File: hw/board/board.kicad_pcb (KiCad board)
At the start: 4 copper layers, 100 x 85 mm, 77 parts, among them J1 Conn_ARM_JTAG_SWD_10, J2 Conn_ARM_JTAG_SWD_10, SW1 TSB008A2526A, SW2 TSB008A2526A, U1 STM32F302CBTx, U2 W25Q128JVSIQTR, U3 AP7361C-18SP-13, U4 AP7361C-10E, U5 TPS54331DR, U6 XC7A35T-FTG256

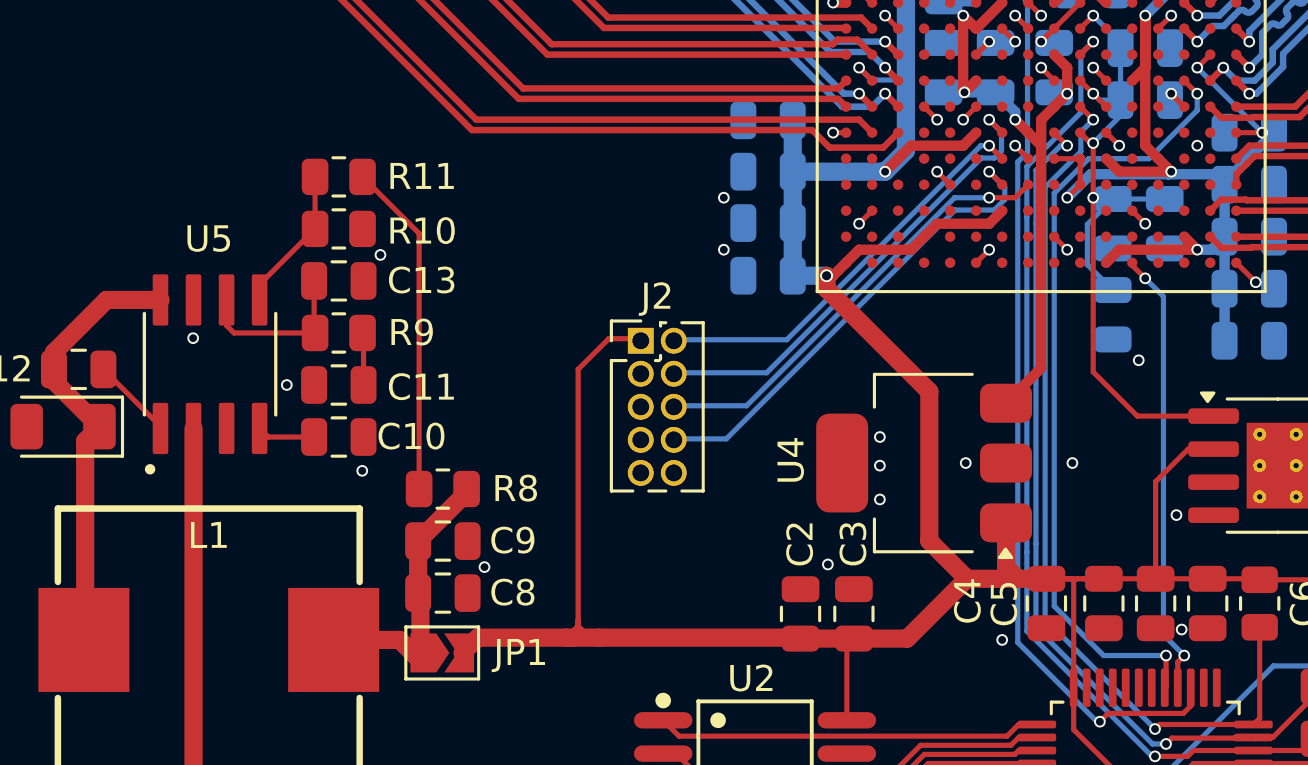
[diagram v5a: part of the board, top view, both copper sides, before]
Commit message: Fixed silkscreen overlaps, updated verilator shims
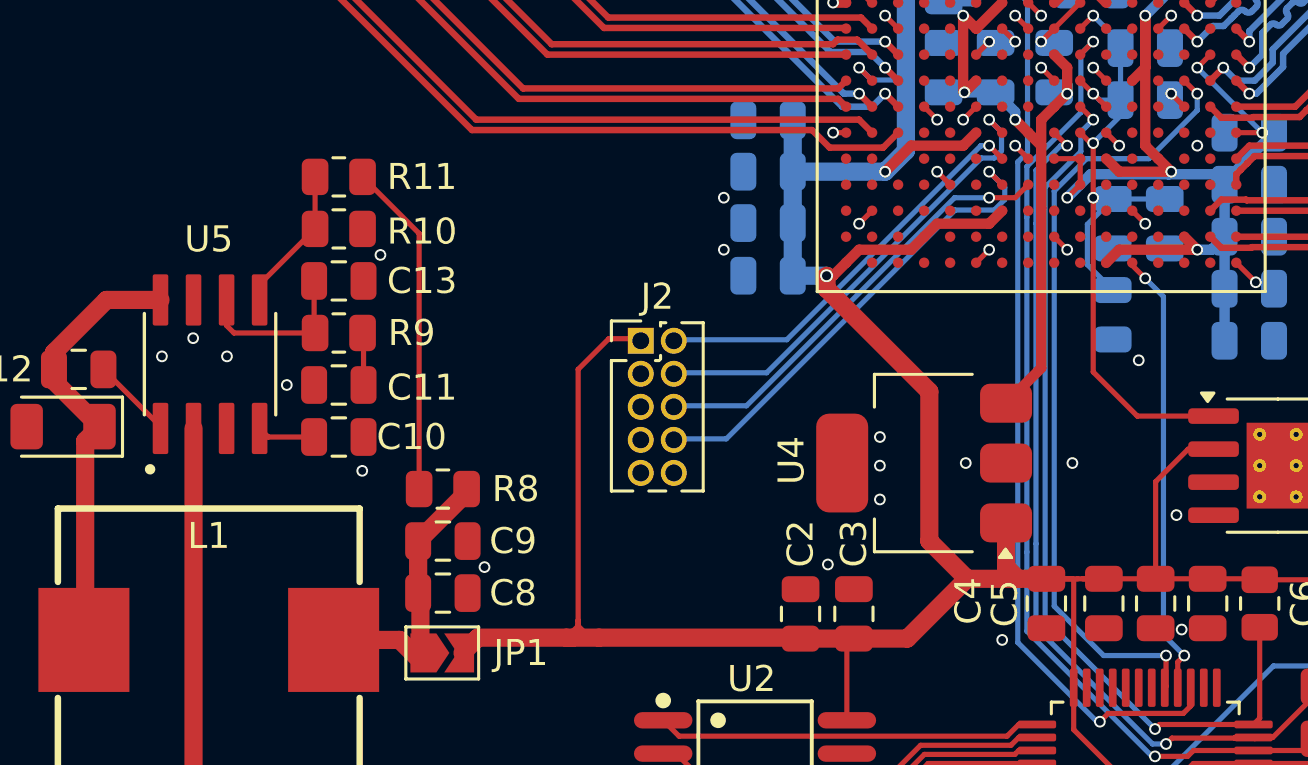
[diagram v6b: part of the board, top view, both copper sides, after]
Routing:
- net GND: vias 55 -> 57
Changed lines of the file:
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@@
 		(tags "capacitor")
 		(property "Reference" "C19"
-			(at 2.75 0 90)
+			(at 3.5 0 90)
 			(layer "B.SilkS")
 			(effects
@@
 		(tags "capacitor")
 		(property "Reference" "C17"
-			(at 2.75 0 0)
+			(at 3.2 0 0)
 			(layer "B.SilkS")
 			(effects
@@
 	)
 	(via
+		(at 102.7 84.1)
+		(size 0.45)
+		(drill 0.3)
+		(layers "F.Cu" "B.Cu")
+		(free yes)
+		(net 5)
+	)
+	(via
 		(at 134 71)
 		(size 0.45)
@@
 	)
 	(via
+		(at 100.2 84.1)
+		(size 0.45)
+		(drill 0.3)
+		(layers "F.Cu" "B.Cu")
+		(free yes)
+		(net 5)
+	)
+	(via
 		(at 147 103.8)
 		(size 0.45)
@@
 	)
 	(segment
-		(start 138.139033 76.5)
-		(end 140 74.639033)
+		(start 135.744974 76.5)
+		(end 138.139033 76.5)
 		(width 0.2)
 		(layer "B.Cu")
@@
 	)
 	(segment
-		(start 138.8 95.6)
-		(end 136.4 95.6)
+		(start 134.5 77.744974)
+		(end 135.744974 76.5)
 		(width 0.2)
 		(layer "B.Cu")
@@
 	)
 	(segment
-		(start 140 74.639033)
-		(end 140 74)
+		(start 138.139033 76.5)
+		(end 140 74.639033)
 		(width 0.2)
 		(layer "B.Cu")
@@
 	)
 	(segment
-		(start 134.5 93.7)
-		(end 134.5 77.828248)
+		(start 138.8 95.6)
+		(end 136.4 95.6)
 		(width 0.2)
 		(layer "B.Cu")
@@
 	)
 	(segment
-		(start 135.828248 76.5)
-		(end 138.139033 76.5)
+		(start 140 74.639033)
+		(end 140 74)
 		(width 0.2)
 		(layer "B.Cu")
@@
 	)
 	(segment
-		(start 134.5 77.828248)
-		(end 135.828248 76.5)
+		(start 134.5 93.7)
+		(end 134.5 77.744974)
 		(width 0.2)
 		(layer "B.Cu")

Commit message: Updated net names for SPI bitstream upload
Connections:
- net CCLK renamed FPGA_CCLK
- net DIN renamed FPGA_DIN
- net DOUT renamed FPGA_DOUT
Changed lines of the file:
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@@
 	(net 40 "unconnected-(U1-PF1-Pad6)")
 	(net 41 "S_{out}5_N")
-	(net 42 "DOUT")
+	(net 42 "FPGA_DOUT")
 	(net 43 "D_{out}5_P")
-	(net 44 "DIN")
+	(net 44 "FPGA_CCLK")
 	(net 45 "unconnected-(U1-PC15-Pad4)")
 	(net 46 "unconnected-(U1-PB7-Pad43)")
@@
 	(net 76 "S_{in}6_P")
 	(net 77 "unconnected-(U6A-IO_L1P_T0_D00_MOSI_14-PadJ13)")
-	(net 78 "CCLK")
+	(net 78 "FPGA_DIN")
 	(net 79 "unconnected-(U6A-IO_L23N_T3_A02_D18_14-PadT5)")
 	(net 80 "D_{in}7_N")
@@
 			(property pad_prop_bga)
 			(layers "F.Cu" "F.Paste" "F.Mask")
-			(net 78 "CCLK")
+			(net 44 "FPGA_CCLK")
 			(pinfunction "CCLK_0")
 			(pintype "bidirectional")
@@
 			(property pad_prop_bga)
 			(layers "F.Cu" "F.Paste" "F.Mask")
-			(net 44 "DIN")
+			(net 78 "FPGA_DIN")
 			(pinfunction "IO_L1N_T0_D01_DIN_14")
 			(pintype "bidirectional")
@@
 			(property pad_prop_bga)
 			(layers "F.Cu" "F.Paste" "F.Mask")
-			(net 42 "DOUT")
+			(net 42 "FPGA_DOUT")
 			(pinfunction "IO_L15N_T2_DQS_DOUT_CSO_B_14")
 			(pintype "bidirectional")
@@
 			(layers "F.Cu" "F.Paste" "F.Mask")
 			(roundrect_rratio 0.25)
-			(net 78 "CCLK")
+			(net 44 "FPGA_CCLK")
 			(pinfunction "PA5")
 			(pintype "bidirectional")
@@
 			(layers "F.Cu" "F.Paste" "F.Mask")
 			(roundrect_rratio 0.25)
-			(net 42 "DOUT")
+			(net 42 "FPGA_DOUT")
 			(pinfunction "PA6")
 			(pintype "bidirectional")
@@
 			(layers "F.Cu" "F.Paste" "F.Mask")
 			(roundrect_rratio 0.25)
-			(net 44 "DIN")
+			(net 78 "FPGA_DIN")
 			(pinfunction "PA7")
 			(pintype "bidirectional")
@@
 	)
 	(segment
-		(start 138.8 95.6)
-		(end 138.8 96.7875)
+		(start 133.5 69.5)
+		(end 133 70)
 		(width 0.2)
 		(layer "F.Cu")
@@
 	)
 	(segment
-		(start 139.5 73.5)
-		(end 140 74)
+		(start 139.75 97.536697)
+		(end 139.75 96.8375)
 		(width 0.2)
 		(layer "F.Cu")
@@
 	)
 	(segment
-		(start 138.8 96.7875)
-		(end 138.75 96.8375)
+		(start 136.256495 98.143505)
+		(end 136.575 97.825)
+		(width 0.2)
+		(layer "F.Cu")
+		(net 44)
+	)
+	(segment
+		(start 139.461697 97.825)
+		(end 139.75 97.536697)
+		(width 0.2)
+		(layer "F.Cu")
+		(net 44)
+	)
+	(segment
+		(start 136.575 97.825)
+		(end 139.461697 97.825)
 		(width 0.2)
 		(layer "F.Cu")
@@
 	)
 	(via
-		(at 138.8 95.6)
+		(at 136.256495 98.143505)
 		(size 0.45)
 		(drill 0.3)
@@
 	)
 	(via
-		(at 140 74)
+		(at 133 70)
 		(size 0.45)
 		(drill 0.3)
@@
 	)
 	(segment
-		(start 135.744974 76.5)
-		(end 138.139033 76.5)
-		(width 0.2)
-		(layer "B.Cu")
-		(net 44)
-	)
-	(segment
-		(start 136.4 95.6)
-		(end 134.5 93.7)
+		(start 133.1 76.625)
+		(end 133.475 76.25)
 		(width 0.2)
 		(layer "B.Cu")
@@
 	)
 	(segment
-		(start 134.5 77.744974)
-		(end 135.744974 76.5)
+		(start 133.1 95.1)
+		(end 133.1 76.625)
 		(width 0.2)
 		(layer "B.Cu")
@@
 	)
 	(segment
-		(start 138.139033 76.5)
-		(end 140 74.639033)
+		(start 136.143505 98.143505)
+		(end 133.1 95.1)
 		(width 0.2)
 		(layer "B.Cu")
@@
 	)
 	(segment
-		(start 138.8 95.6)
-		(end 136.4 95.6)
+		(start 136.256495 98.143505)
+		(end 136.143505 98.143505)
 		(width 0.2)
 		(layer "B.Cu")
@@
 	)
 	(segment
-		(start 140 74.639033)
-		(end 140 74)
+		(start 133.475 76.25)
+		(end 133.475 70.475)
 		(width 0.2)
 		(layer "B.Cu")
@@
 	)
 	(segment
-		(start 134.5 93.7)
-		(end 134.5 77.744974)
+		(start 133.475 70.475)
+		(end 133 70)
 		(width 0.2)
 		(layer "B.Cu")
@@
 	)
 	(segment
-		(start 133.5 69.5)
-		(end 133 70)
-		(width 0.2)
-		(layer "F.Cu")
-		(net 78)
-	)
-	(segment
-		(start 139.75 97.536697)
-		(end 139.75 96.8375)
-		(width 0.2)
-		(layer "F.Cu")
-		(net 78)
-	)
-	(segment
-		(start 136.256495 98.143505)
-		(end 136.575 97.825)
+		(start 138.8 95.6)
+		(end 138.8 96.7875)
 		(width 0.2)
 		(layer "F.Cu")
@@
 	)
 	(segment
-		(start 139.461697 97.825)
-		(end 139.75 97.536697)
+		(start 139.5 73.5)
+		(end 140 74)
 		(width 0.2)
 		(layer "F.Cu")
@@
 	)
 	(segment
-		(start 136.575 97.825)
-		(end 139.461697 97.825)
+		(start 138.8 96.7875)
+		(end 138.75 96.8375)
 		(width 0.2)
 		(layer "F.Cu")
@@
 	)
 	(via
-		(at 136.256495 98.143505)
+		(at 138.8 95.6)
 		(size 0.45)
 		(drill 0.3)
@@
 	)
 	(via
-		(at 133 70)
+		(at 140 74)
 		(size 0.45)
 		(drill 0.3)
@@
 	)
 	(segment
-		(start 133.1 76.625)
-		(end 133.475 76.25)
+		(start 135.744974 76.5)
+		(end 138.139033 76.5)
 		(width 0.2)
 		(layer "B.Cu")
@@
 	)
 	(segment
-		(start 133.1 95.1)
-		(end 133.1 76.625)
+		(start 136.4 95.6)
+		(end 134.5 93.7)
 		(width 0.2)
 		(layer "B.Cu")
@@
 	)
 	(segment
-		(start 136.143505 98.143505)
-		(end 133.1 95.1)
+		(start 134.5 77.744974)
+		(end 135.744974 76.5)
 		(width 0.2)
 		(layer "B.Cu")
@@
 	)
 	(segment
-		(start 136.256495 98.143505)
-		(end 136.143505 98.143505)
+		(start 138.139033 76.5)
+		(end 140 74.639033)
 		(width 0.2)
 		(layer "B.Cu")
@@
 	)
 	(segment
-		(start 133.475 76.25)
-		(end 133.475 70.475)
+		(start 138.8 95.6)
+		(end 136.4 95.6)
 		(width 0.2)
 		(layer "B.Cu")
@@
 	)
 	(segment
-		(start 133.475 70.475)
-		(end 133 70)
+		(start 140 74.639033)
+		(end 140 74)
+		(width 0.2)
+		(layer "B.Cu")
+		(net 78)
+	)
+	(segment
+		(start 134.5 93.7)
+		(end 134.5 77.744974)
 		(width 0.2)
 		(layer "B.Cu")

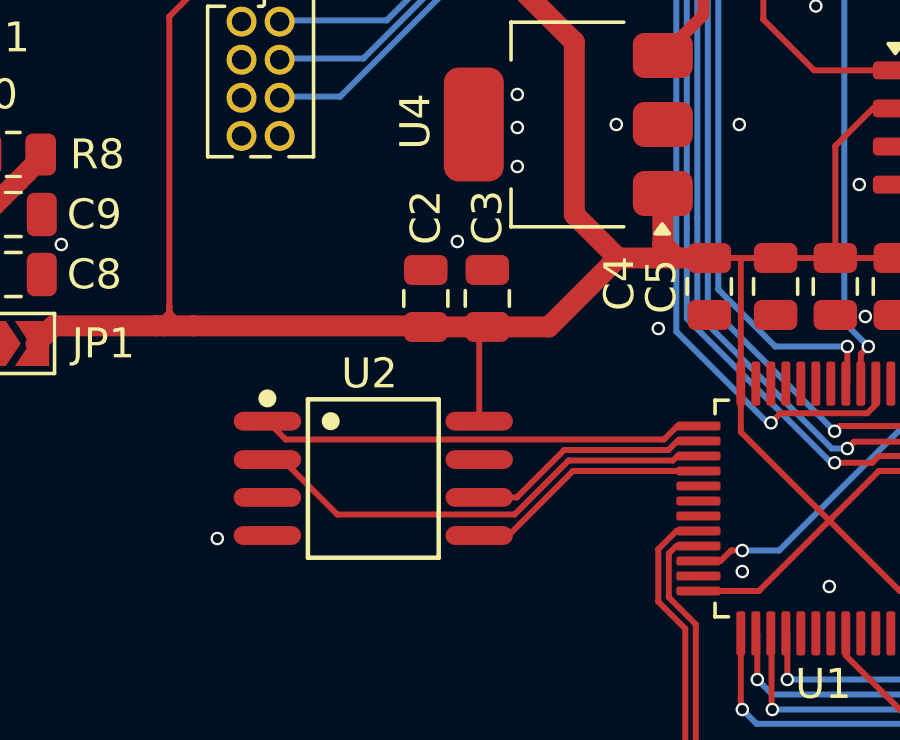
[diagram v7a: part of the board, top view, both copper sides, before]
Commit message: Reduced flash size
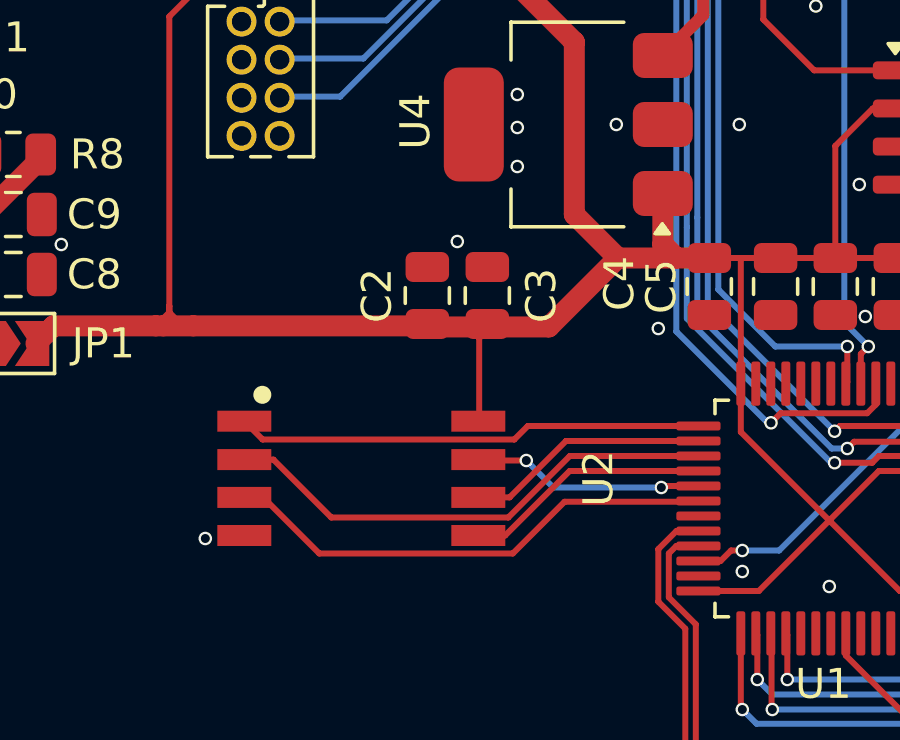
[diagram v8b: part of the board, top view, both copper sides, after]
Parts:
- U2: value W25Q128JVSIQTR -> IS25LP064D-JBLE-TR; footprint EasyEDA:SOIC-8_L5.3-W5.3-P1.27-LS8.0-BL -> EasyEDA:SOIC-8_L5.3-W5.3-P1.27-LS7.9-BL
- moved U2 0.40 mm to (122.6, 100.0)
- moved C2 0.11 mm to (124.8, 93.9)
- moved C3 0.10 mm to (126.8, 93.9)
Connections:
- U1 pad 29: unconnected-(U1-PA8-Pad29) -> FLASH_HOLD
- U1 pad 30: unconnected-(U1-PA9-Pad30) -> FLASH_WP
- U2 pad 3: unconnected-(U2-IO2-Pad3) -> FLASH_WP
- U2 pad 7: unconnected-(U2-IO3-Pad7) -> FLASH_HOLD
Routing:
- net FLASH_WP: track 0.00 -> 17.3 mm
- net FLASH_HOLD: track 0.00 -> 7.74 mm, vias 0 -> 2
- net FLASH_MISO: track 15.9 -> 16.8 mm
- net ~{FLASH_CS}: track 14.8 -> 15.6 mm
- net unconnected-(U1-PA9-Pad30): track 0.62 -> 0.00 mm
